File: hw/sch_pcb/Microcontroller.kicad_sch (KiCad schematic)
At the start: 32 parts

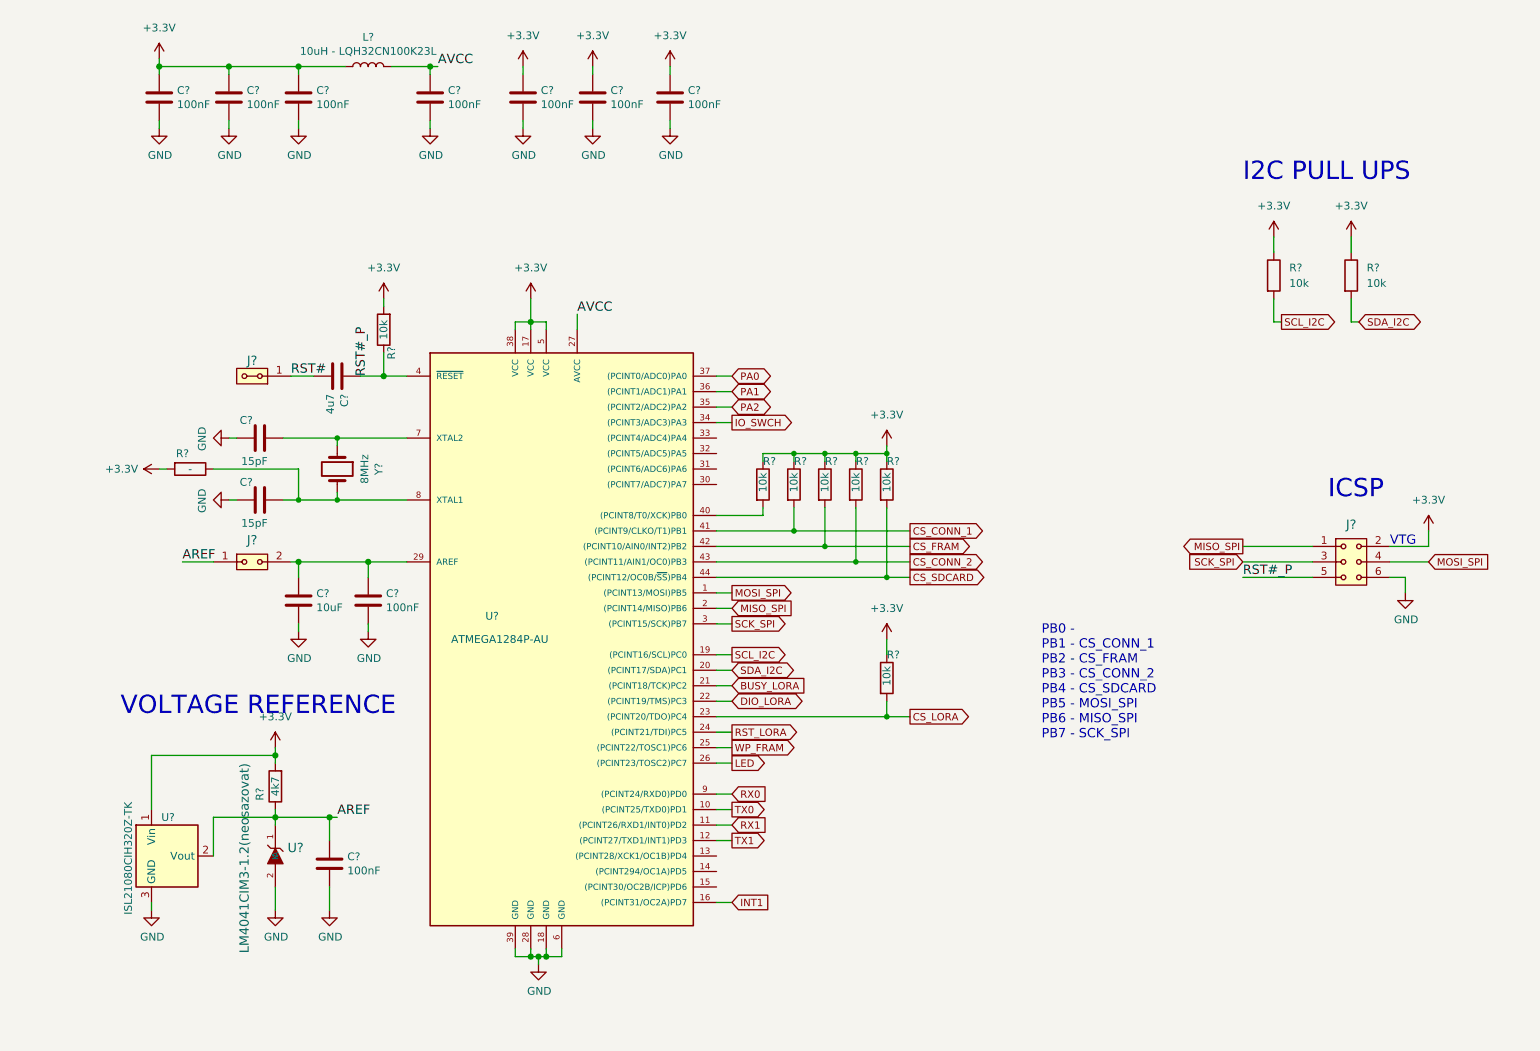
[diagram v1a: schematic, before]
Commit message: schematics update
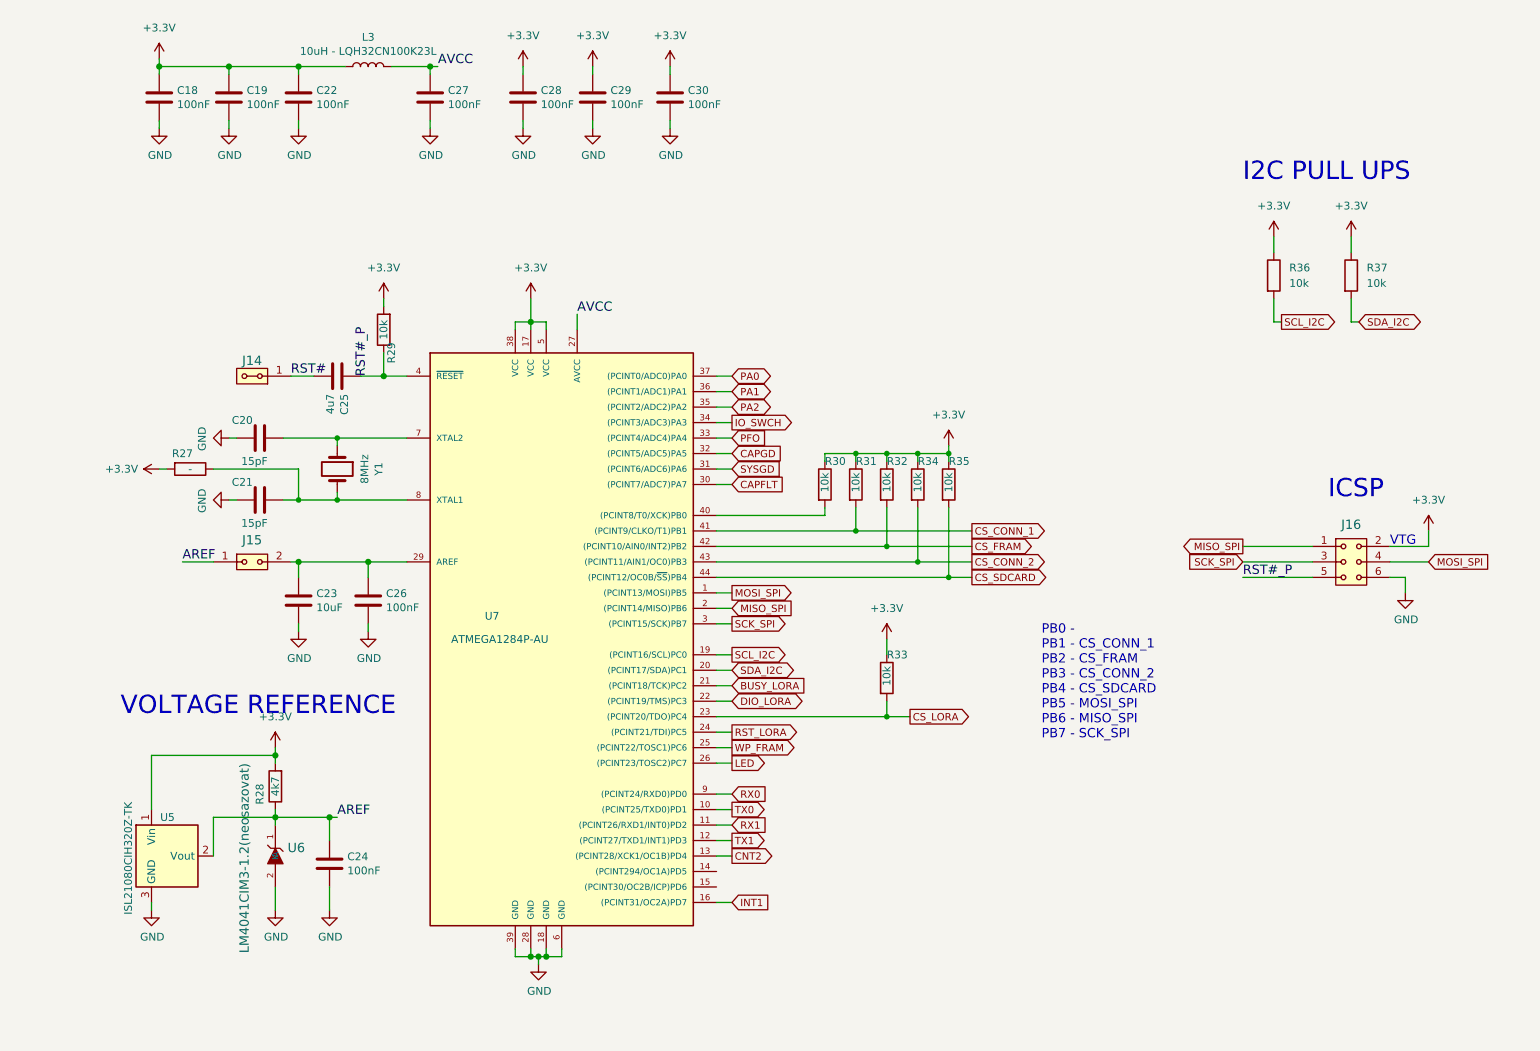
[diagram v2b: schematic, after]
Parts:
- gave numbers to parts that had none: 32
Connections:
- net CNT2: now reaches U7.13 ((PCINT28/XCK1/OC1B)PD4)
- net CAPFLT: now reaches U7.30 ((PCINT7/ADC7)PA7)
- net SYSGD: now reaches U7.31 ((PCINT6/ADC6)PA6)
- net CAPGD: now reaches U7.32 ((PCINT5/ADC5)PA5)
- net PFO: now reaches U7.33 ((PCINT4/ADC4)PA4)
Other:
- moved on the sheet: R30, R31, R32, R34, R35

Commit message: schematics update
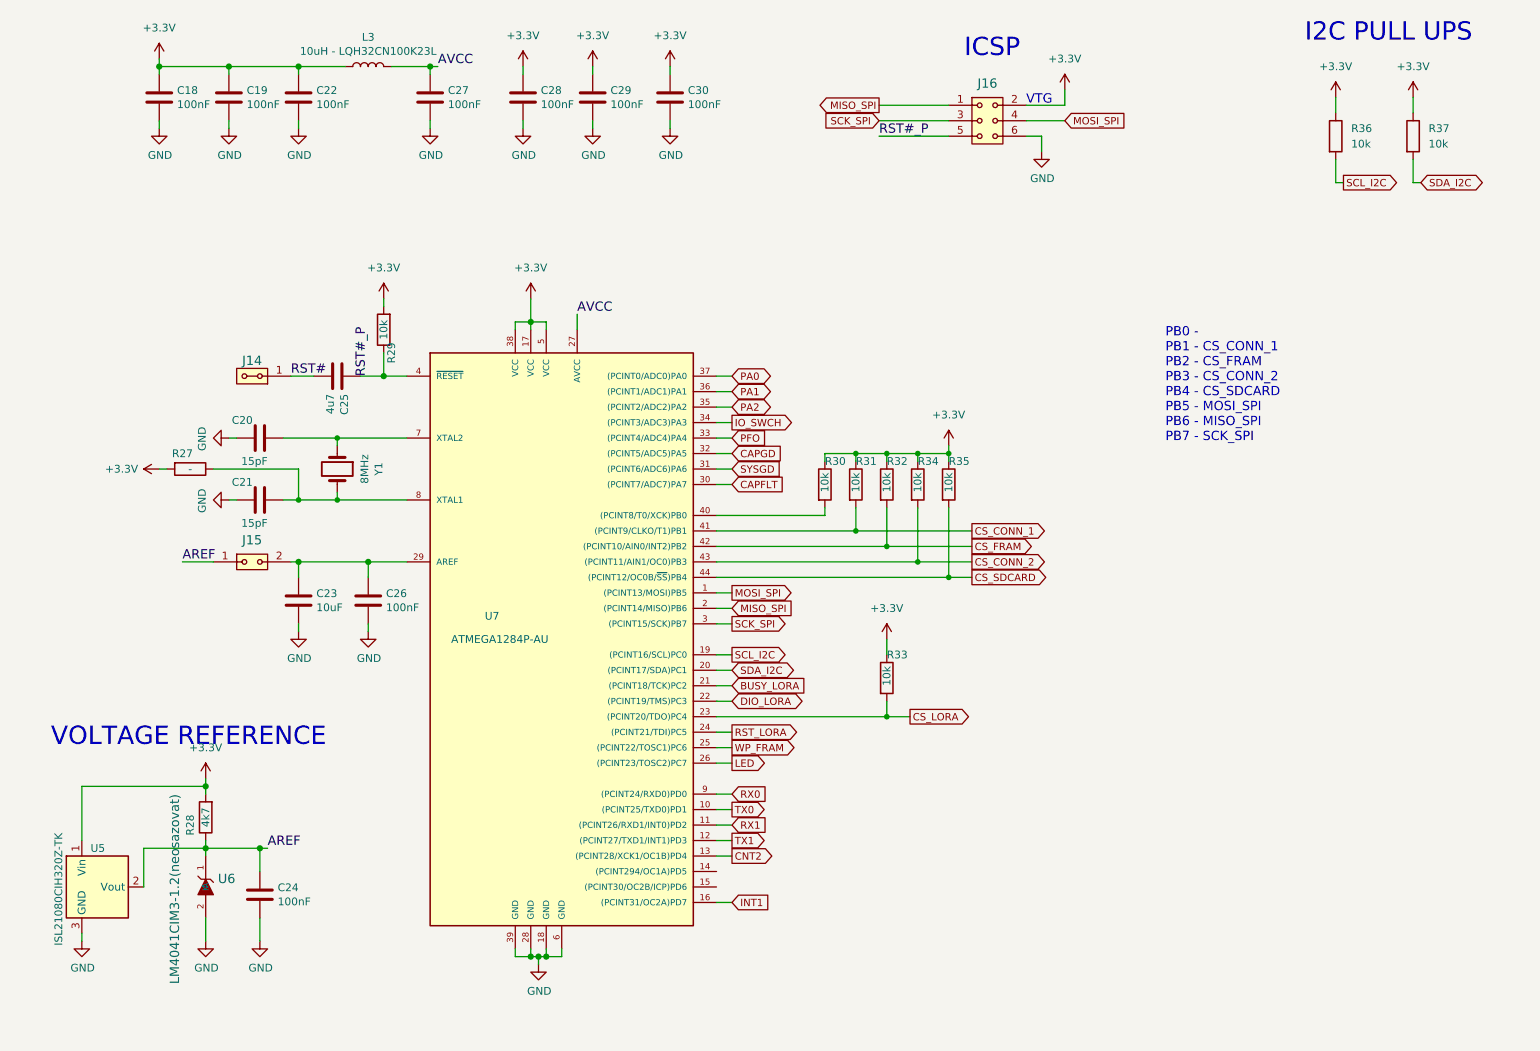
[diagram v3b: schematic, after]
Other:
- moved on the sheet: C24, J16, R28, R36, R37, U5, U6

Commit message: progress?
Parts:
- removed C28, C29, C30: 100nF, Mlab_R:SMD-0805, symbol DATALOGGER01A-rescue:C-device
- removed R30, R33: 10k, symbol Device:R
- removed Y1: 8MHz, Mlab_XTAL:Crystal_HC49-U_Vertical, symbol Device:Crystal
- added R48: 10k, Mlab_R:SMD-0805, symbol Device:R
- added Y6: 8MHz LFXTAL083138, Mlab_XTAL:Crystal SMD CFPX-180, symbol Device:Crystal_GND24
- C1: renamed from C18; footprint Mlab_R:SMD-0805 -> Mlab_C:SMD-0805
- C10: renamed from C27; footprint Mlab_R:SMD-0805 -> Mlab_C:SMD-0805
- C2: renamed from C19; footprint Mlab_R:SMD-0805 -> Mlab_C:SMD-0805
- C3: renamed from C20; footprint Mlab_R:SMD-0805 -> Mlab_C:SMD-0805
- C4: renamed from C21; footprint Mlab_R:SMD-0805 -> Mlab_C:SMD-0805
- C5: renamed from C24; footprint Mlab_R:SMD-0805 -> Mlab_C:SMD-0805
- C6: renamed from C22; footprint Mlab_R:SMD-0805 -> Mlab_C:SMD-0805
- C7: renamed from C23; footprint Mlab_R:SMD-0805 -> Mlab_C:SMD-0805
- C8: renamed from C25; footprint Mlab_R:SMD-0805 -> Mlab_C:SMD-0805
- C9: renamed from C26; footprint Mlab_R:SMD-0805 -> Mlab_C:SMD-0805
- R10: renamed from R36; footprint (none) -> Mlab_R:SMD-0805
- R11: renamed from R37; footprint (none) -> Mlab_R:SMD-0805
- R5: renamed from R31; footprint (none) -> Mlab_R:SMD-0805
- R6: renamed from R32; footprint (none) -> Mlab_R:SMD-0805
- R8: renamed from R34; footprint (none) -> Mlab_R:SMD-0805
- R9: renamed from R35; footprint (none) -> Mlab_R:SMD-0805
- renumbered J14 to J1, J15 to J2, J16 to J3, L3 to L1, R27 to R1, R28 to R2, R29 to R3, U5 to U1, U6 to U2, U7 to U3
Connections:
- net +3.3V: now also R48.1
- net BUSY_LORA: now also U3.32 ((PCINT5/ADC5)PA5); no longer U3.21 ((PCINT18/TCK)PC2)
- net CAPFLT: now also U3.24 ((PCINT21/TDI)PC5); no longer U3.30 ((PCINT7/ADC7)PA7)
- net CAPGD: now also U3.22 ((PCINT19/TMS)PC3); no longer U3.32 ((PCINT5/ADC5)PA5)
- net CS_LORA: now also U3.33 ((PCINT4/ADC4)PA4), R48.2; no longer U3.23 ((PCINT20/TDO)PC4)
- net DIO_LORA: now also U3.31 ((PCINT6/ADC6)PA6); no longer U3.22 ((PCINT19/TMS)PC3)
- net GND: now also Y6.2, Y6.4
- net PFO: now also U3.21 ((PCINT18/TCK)PC2); no longer U3.33 ((PCINT4/ADC4)PA4)
- net RST_LORA: now also U3.30 ((PCINT7/ADC7)PA7); no longer U3.24 ((PCINT21/TDI)PC5)
- net SYSGD: now also U3.23 ((PCINT20/TDO)PC4); no longer U3.31 ((PCINT6/ADC6)PA6)
- net WP_FRAM: now also U3.40 ((PCINT8/T0/XCK)PB0); no longer U3.25 ((PCINT22/TOSC1)PC6)
- net at C3.2, U3.7 (XTAL2): now also Y6.3
- net at C4.2, R1.1, U3.8 (XTAL1): now also Y6.1

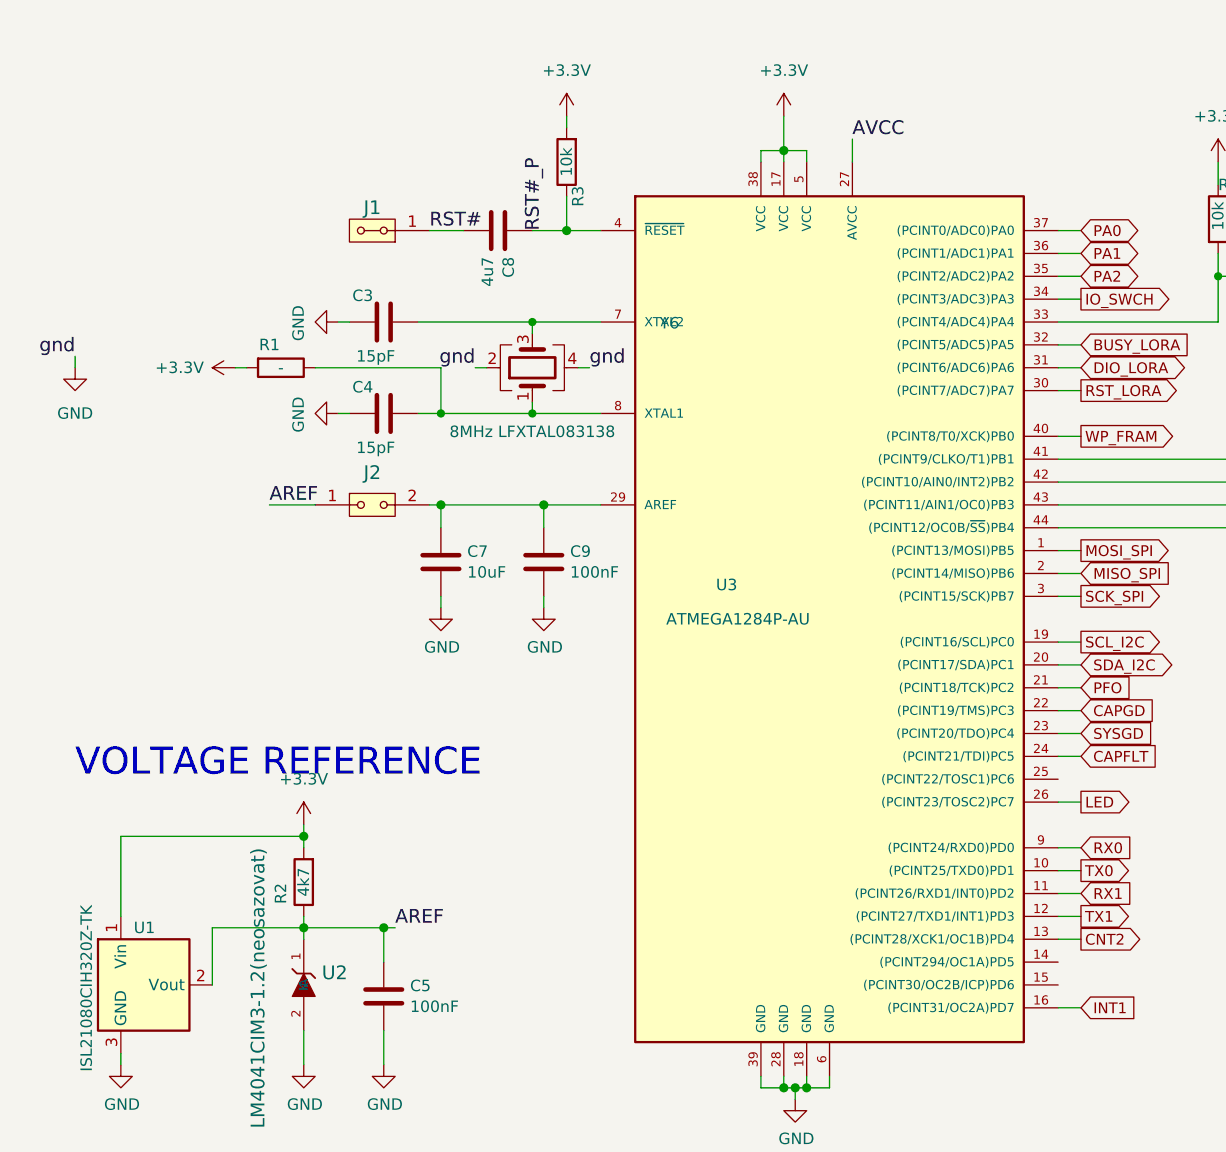
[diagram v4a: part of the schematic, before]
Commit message: Update components from libraries. Improve schematics. Resolve some ERC and DRC errors.
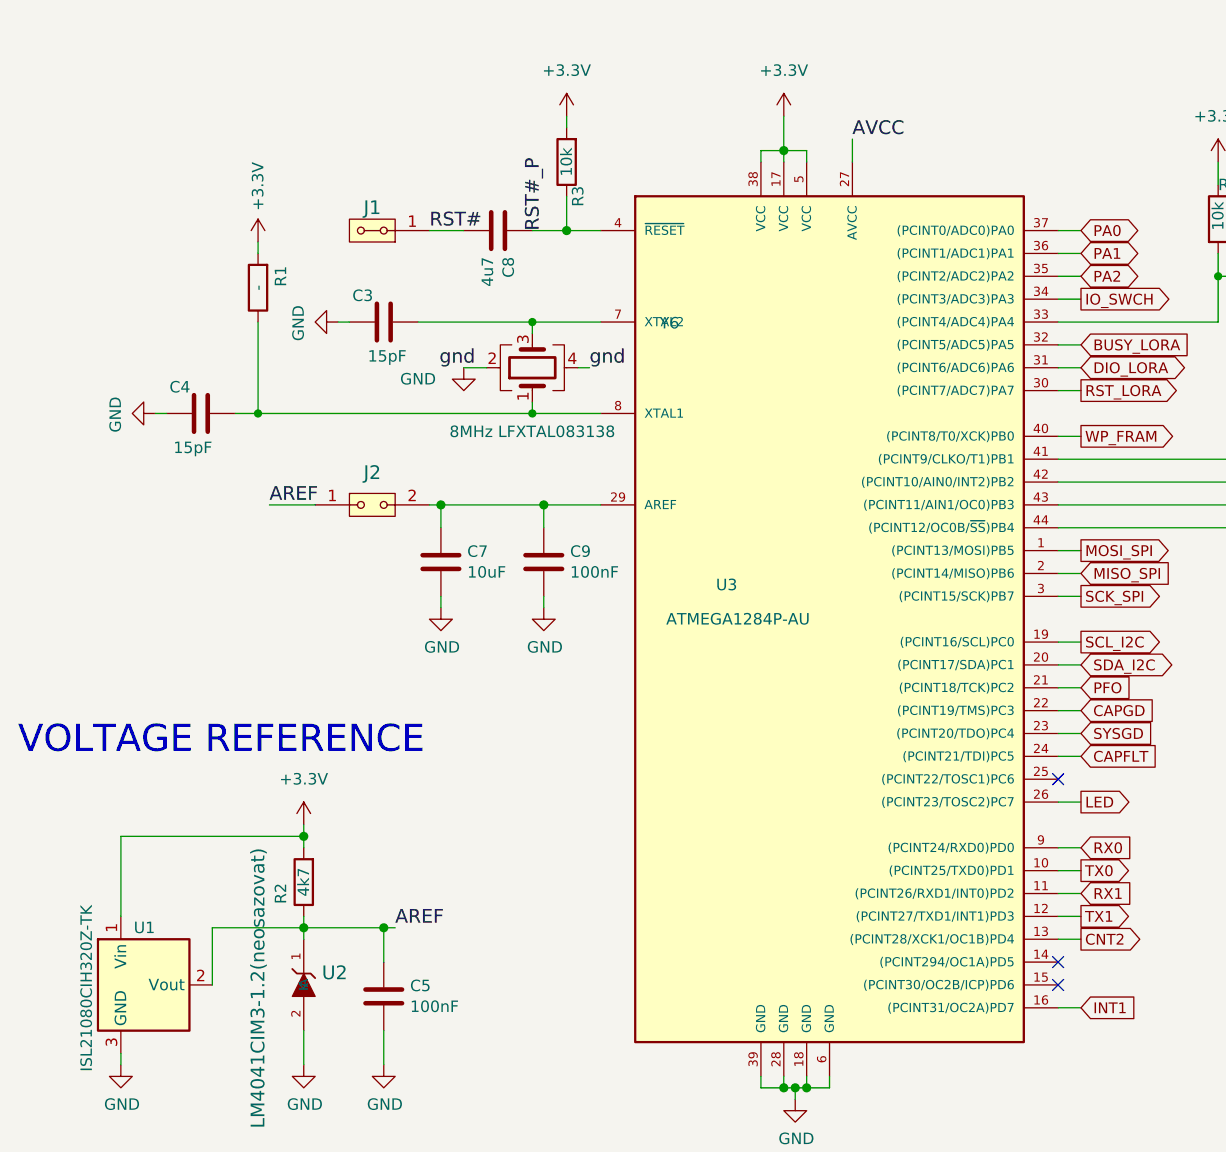
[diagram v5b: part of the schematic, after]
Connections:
- no-connect marks 0 -> 3
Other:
- moved on the sheet: C4, R1
